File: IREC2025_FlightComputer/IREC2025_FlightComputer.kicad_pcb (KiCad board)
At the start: 4 copper layers, 63.6 x 117.5 mm, 150 parts, among them J1 Molex Microfit, J2 BOOT0, J3 Companion, J5 SWD, Q1 SI7232DN-T1-GE3, U1 STM32U575VGTx, U10 PE4259-63, U11 SX1262IMLTRT, U12 ADXL375BCCZ-RL7, U13 MMC5983MA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

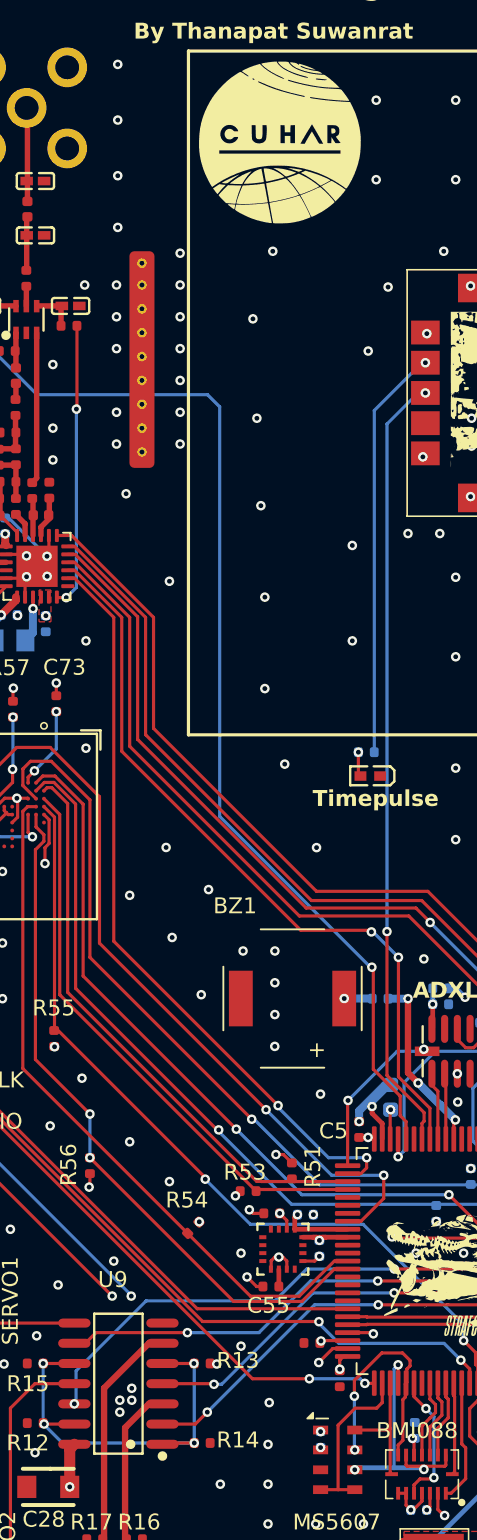
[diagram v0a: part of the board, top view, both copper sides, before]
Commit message: Schematics minor fixes
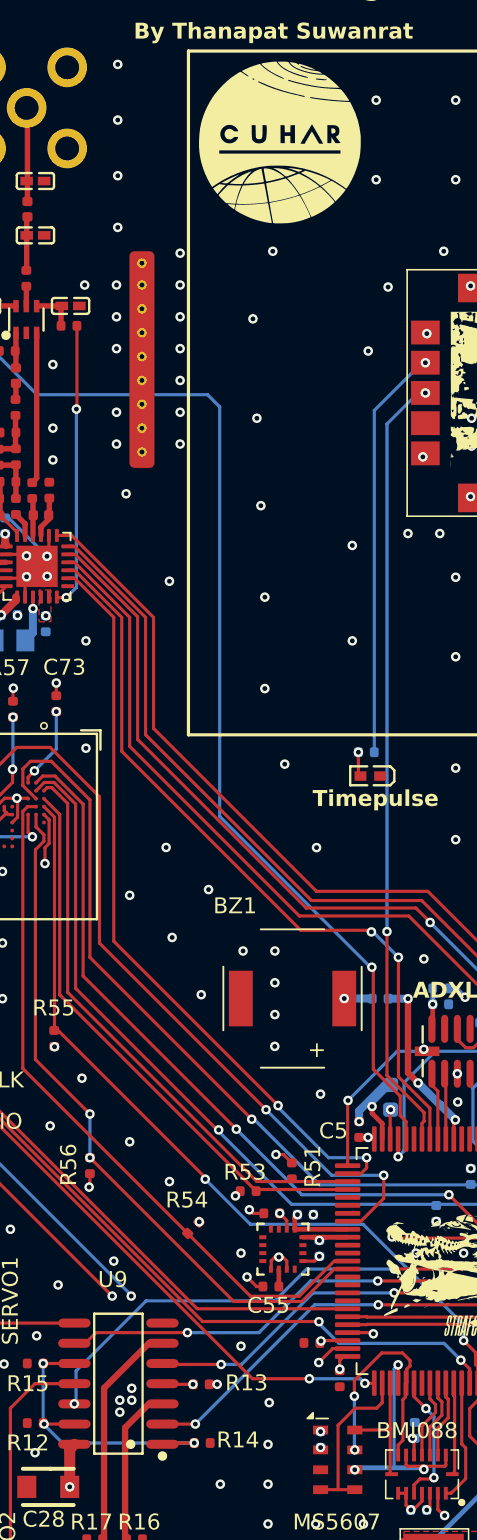
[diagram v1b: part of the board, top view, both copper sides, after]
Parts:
- moved R13 1.31 mm to (79.0, 115.8)
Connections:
- U9 pad 4: PWM_B -> /PWM_PD
- U9 pad 5: /PWM_PD -> PWM_B
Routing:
- net /PWM_PD: track 26.8 -> 21.8 mm
- net PWM_B: track 30.6 -> 30.1 mm
- net VBAT-: track 117.9 -> 118.0 mm, vias 278 -> 282

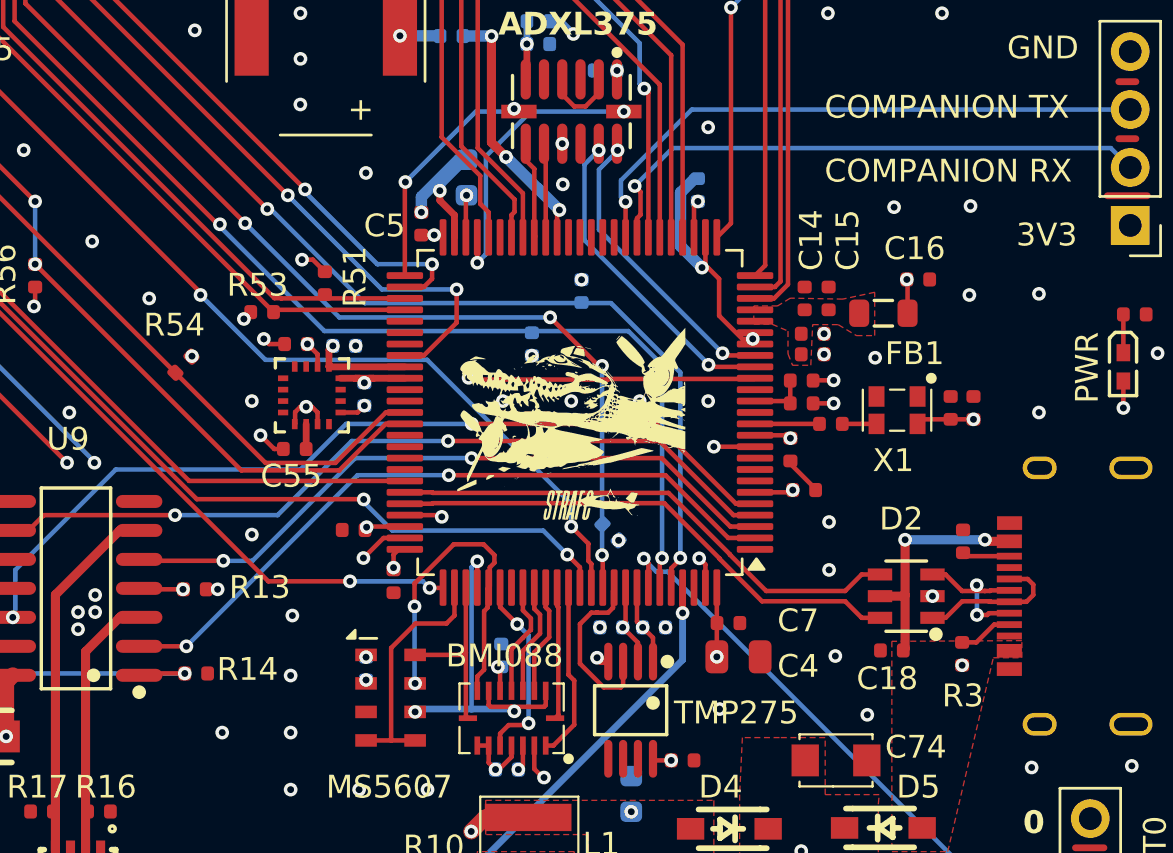
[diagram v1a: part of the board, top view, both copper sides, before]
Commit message: USB Differentials matched to 90R
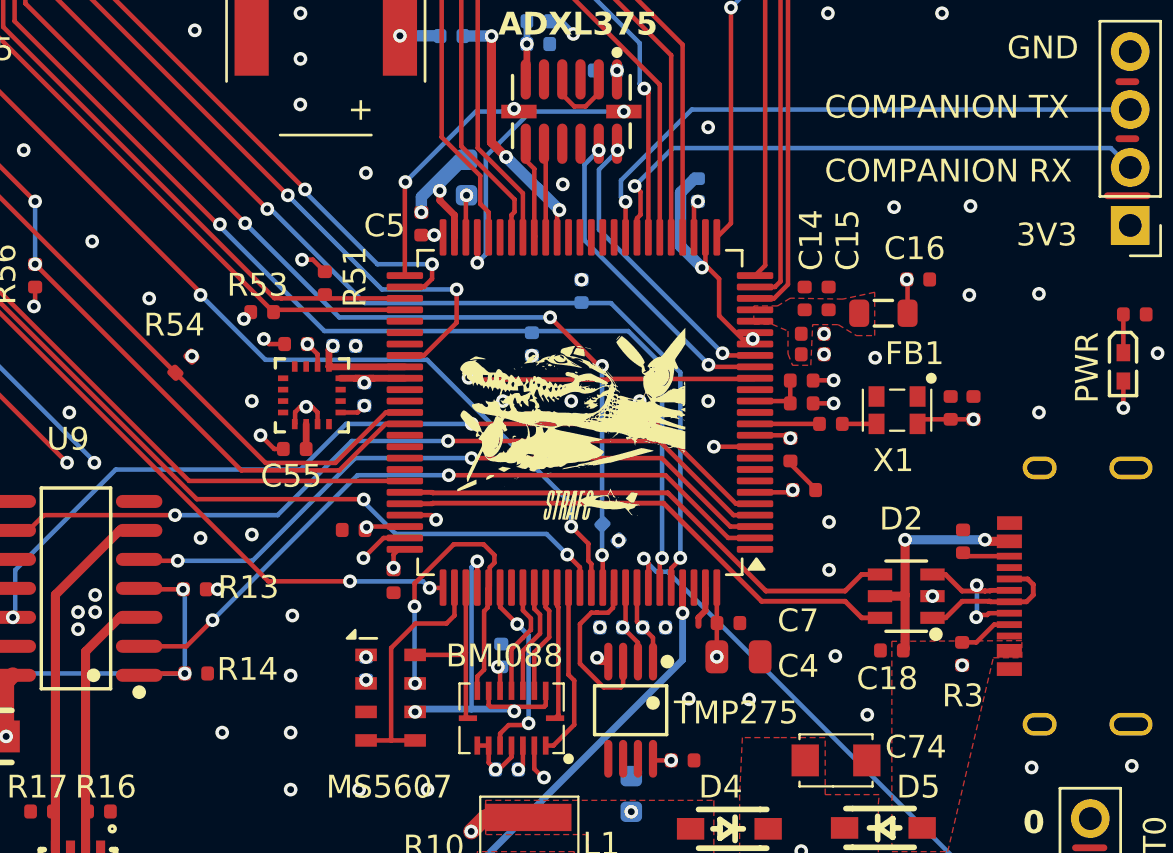
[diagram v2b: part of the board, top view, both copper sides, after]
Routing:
- net /PWM_PD: track 21.8 -> 25.5 mm

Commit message: forgor mmc int :( added
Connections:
- U1 pad 61: unconnected-(U1-PD14-Pad61) -> MMC_INT
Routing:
- net MMC_INT: track 0.00 -> 7.23 mm, vias 0 -> 2
